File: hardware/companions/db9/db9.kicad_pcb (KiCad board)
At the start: 2 copper layers, 28.1 x 14 mm, 9 parts, among them J1 edge10, J2 edge10, J3 DB9_Male, J4 edge10, Q1 BSS138, Q2 BSS138

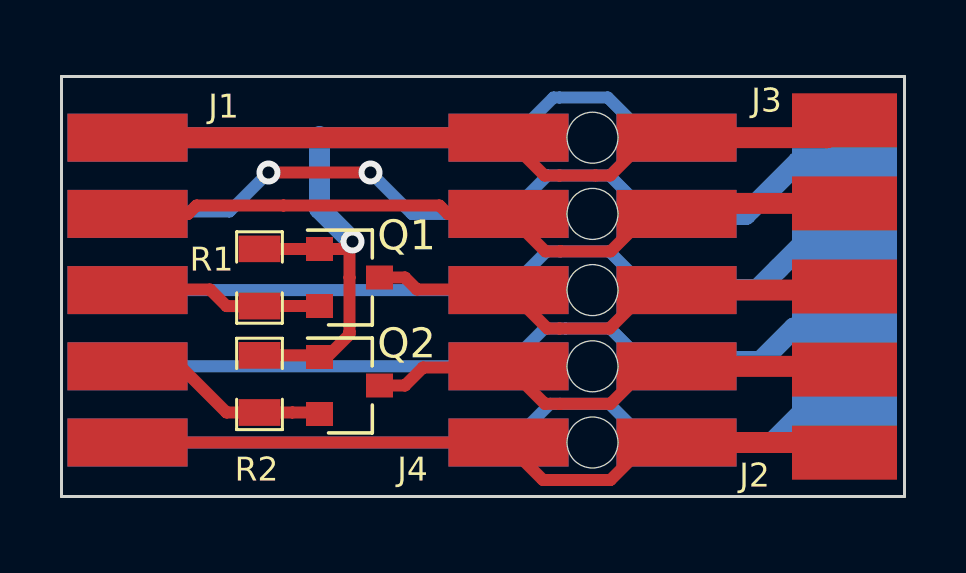
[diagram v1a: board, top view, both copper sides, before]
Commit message: Added wiring diagram, increased PCB size
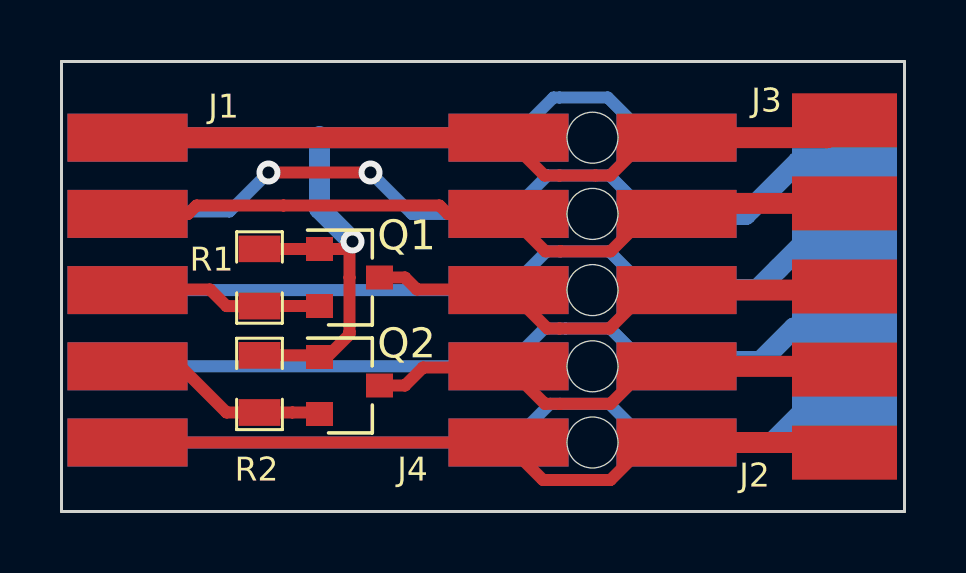
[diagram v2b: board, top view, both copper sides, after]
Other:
- board size 28.1 x 14 mm -> 28.1 x 15 mm
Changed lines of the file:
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@@
   (general
     (thickness 1.6)
-    (drawings 4)
+    (drawings 9)
     (tracks 134)
     (zones 0)
@@
     (pad_to_mask_clearance 0)
     (solder_mask_min_width 0.25)
-    (aux_axis_origin 142.9 61)
+    (aux_axis_origin 142.9 60.5)
     (visible_elements FFFFFF7F)
     (pcbplotparams
@@
     (pad "" np_thru_hole circle (at 0 0) (size 1.7 1.7) (drill 1.7) (layers *.Cu *.Mask))
   )
-  (gr_line (start 142.9 75) (end 171 75) (layer Edge.Cuts) (width 0.1))
+  (gr_line (start 142.9 60.5) (end 142.9 61) (layer Edge.Cuts) (width 0.1))
+  (gr_line (start 171 60.5) (end 142.9 60.5) (layer Edge.Cuts) (width 0.1))
+  (gr_line (start 171 61) (end 171 60.5) (layer Edge.Cuts) (width 0.1))
+  (gr_line (start 171 75.5) (end 148.7 75.5) (layer Edge.Cuts) (width 0.1))
+  (gr_line (start 171 75) (end 171 75.5) (layer Edge.Cuts) (width 0.1))
+  (gr_line (start 142.9 75.5) (end 148.7 75.5) (layer Edge.Cuts) (width 0.1))
+  (gr_line (start 142.9 75) (end 142.9 75.5) (layer Edge.Cuts) (width 0.1))
   (gr_line (start 142.9 61) (end 142.9 75) (layer Edge.Cuts) (width 0.1))
-  (gr_line (start 171 61) (end 142.9 61) (layer Edge.Cuts) (width 0.1))
   (gr_line (start 171 75) (end 171 61) (layer Edge.Cuts) (width 0.1))
   (segment (start 162.450002 63.04) (end 161.110002 61.7) (width 0.4) (layer B.Cu) (net 1))
